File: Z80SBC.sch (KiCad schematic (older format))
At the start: 52 parts, among them IC1 SIO2-DIP-40, IC2 Z80CPU-DIP, J1 PH, J2 DB9_Female, J3 CFCONN, J4 Barrel_Jack, SW1 SW_Push, SW2 SW_Push, U1 MAX232_ALT, U2 74LS138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

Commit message: revised README.md
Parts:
- removed C13: 100 nF, Capacitors_THT:C_Disc_D5.0mm_W2.5mm_P5.00mm, symbol C_Small
- removed JP2: HCT/TTL, Pin_Headers:Pin_Header_Straight_1x03_Pitch2.54mm, symbol Jumper_NC_Dual
- removed R11: R, Resistors_THT:R_Axial_DIN0207_L6.3mm_D2.5mm_P7.62mm_Horizontal, symbol R
- removed R12: 1k, Resistors_THT:R_Axial_DIN0207_L6.3mm_D2.5mm_P7.62mm_Horizontal, symbol R
- removed U4: 27128, symbol 27128
- added C20, C21, C22, C23, C24, C25: 100 nF, Capacitors_THT:C_Disc_D5.0mm_W2.5mm_P2.50mm, symbol C_Small
- added JP6: Jumper_NC_Dual, Pin_Headers:Pin_Header_Straight_1x03_Pitch2.54mm, symbol Jumper_NC_Dual
- added U4: 28C256, Housings_DIP:DIP-28_W15.24mm_Socket, symbol 28C256
- C10, C11, C12, C8, C9: footprint Capacitors_THT:C_Disc_D5.0mm_W2.5mm_P5.00mm -> Capacitors_THT:C_Disc_D5.0mm_W2.5mm_P2.50mm
- C5, C6: value C -> 22 pF
- J3: footprint Pin_Headers:Pin_Header_Straight_2x25_Pitch1.27mm -> Z80:Pin_Header_Straight_2x25_Pitch1.27mm_Rev
- J4: footprint (none) -> Connectors:BARREL_JACK
- R6: value R -> 1M
- U1, U2: footprint (none) -> Housings_DIP:DIP-16_W7.62mm_Socket
- U6, U8: value 74LS32 -> 74HCT32
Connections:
- net labels added: IO08-0F, IO18-1F, IO20-27, IO28-2F, IO30-37, VCC
- net labels removed: ENABLEROM
- wire segments 285 -> 249
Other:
- note added: "Z80 CPM COMPUTER SYSTEM\nBASED ON 9 CHIP CP/M COMPUTER BY GRANT SEARLE\n"
- note removed: "R6/R11 1 M 74HCT00 / 330 ohm 74LS00\nC5 22 pF 74HCT 00/ 120 pF 74LS00\nC6 22 pF 74HCT00 / NC 74LS00\nJP2 1-2 74HCT00 / 2-3 74LS00"
- note removed: "Z80 CPM COMPUTER SYSTEM\n9 CHIP\nORIGINAL DESIGN BY GRANT SEARLE\n"
- moved on the sheet: C5, C6, R6, U2, U6A, U6B, U6C, U6D, U7A, U7B, U7C, U7D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

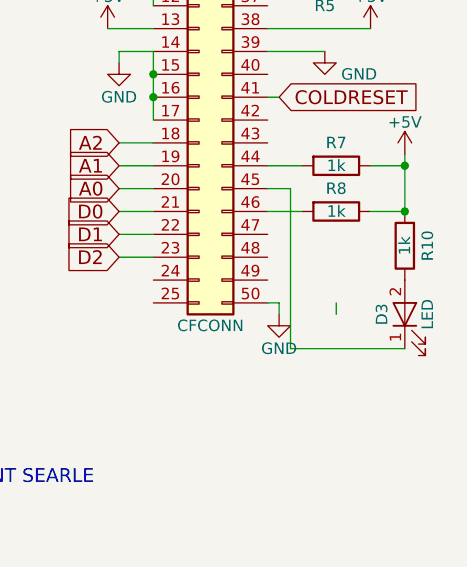
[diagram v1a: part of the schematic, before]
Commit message: Added PS/2 keyboard input
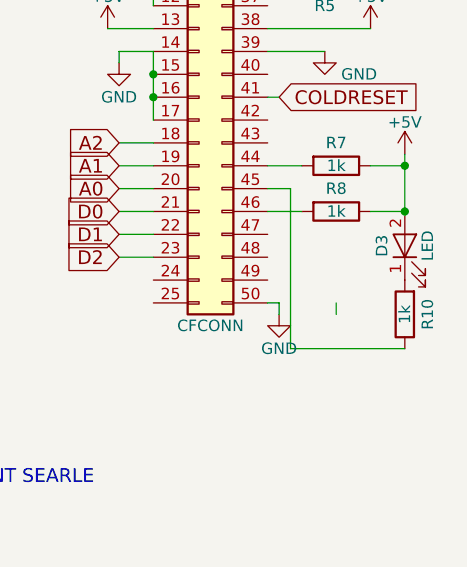
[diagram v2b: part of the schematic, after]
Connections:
- net +5V: now also D3.2 (A); no longer R10.2
- net at J3.45 (Pin_45): now also R10.1; no longer D3.1 (K)
- new net: D3.1 (K), R10.2
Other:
- moved on the sheet: D3, R10

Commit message: Added ESP-01 and video output
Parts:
- removed IC1: SIO2-DIP-40, Housings_DIP:DIP-40_W15.24mm_Socket, symbol SIO2-DIP-40
- added C32: 100 nF, Capacitors_THT:C_Disc_D5.0mm_W2.5mm_P2.50mm, symbol C_Small
- added D10, D9: 1N4148, Diodes_THT:D_DO-35_SOD27_P7.62mm_Horizontal, symbol D
- added IC1: DART-DIP-40, Housings_DIP:DIP-40_W15.24mm_Socket, symbol DART-DIP-40
- added J15: Conn_02x04_Odd_Even, Z80:Pin_Header_Straight_2x04_Pitch2.54mm_Flipped, symbol Conn_02x04_Odd_Even
- added JP7: Jumper_NC_Dual, Pin_Headers:Pin_Header_Straight_1x03_Pitch2.54mm, symbol Jumper_NC_Dual
- added R32: 470R, Resistors_THT:R_Axial_DIN0207_L6.3mm_D2.5mm_P7.62mm_Horizontal, symbol R
- added R33: 1k, Resistors_THT:R_Axial_DIN0207_L6.3mm_D2.5mm_P7.62mm_Horizontal, symbol R
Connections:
- net +5V: now also D9.2 (A), IC1.6 (IEI), IC1.9 (+5V), JP7.3
- net A0: now also IC1.34 (B/~A)
- net A1: now also IC1.33 (C/~D)
- net A14: now also JP7.1; no longer U4.1 (A14)
- net CLK: now also IC1.13 (~RXCA), IC1.14 (~TXCA), IC1.20 (Φ), IC1.27 (~RxTxCB)
- net COLDRESET: now also IC1.21 (~RESET)
- net D0: now also IC1.40 (D0)
- net D1: now also IC1.1 (D1)
- net D2: now also IC1.39 (D2)
- net D3: now also IC1.2 (D3)
- net D4: now also IC1.38 (D4)
- net D5: now also IC1.3 (D5)
- net D6: now also IC1.37 (D6)
- net D7: now also IC1.4 (D7)
- net GND: now also C32.2, IC1.19 (~DCDA), IC1.22 (~DCDB), IC1.23 (~CTSB), IC1.31 (GND), J15.1 (Pin_1), R33.1
- net INT: now also IC1.5 (~INT)
- net IO00-07: now also IC1.35 (~CE)
- net IORQ: now also IC1.36 (~IORQ)
- net M1: now also IC1.8 (~M1)
- net RD: now also IC1.32 (~RD)
- net RTSB: now also IC1.24 (~RTSB)
- net RXDB: now also IC1.28 (RXDB)
- net TXDB: now also IC1.26 (TXDB)
- net at J1.6 (Pin_6): now also IC1.12 (RXDA), J15.2 (Pin_2)
- net at J1.5 (Pin_5): now also IC1.15 (TXDA), R32.2
- net at J1.2 (Pin_2): now also IC1.16 (~DTRA)
- net at J1.4 (Pin_4): now also IC1.17 (~RTSA)
- net at J1.3 (Pin_3), JP1.2: now also IC1.18 (~CTSA)
- new net: J15.7 (Pin_7), R32.1, R33.2
- new net: C32.1, D10.1 (K), J15.8 (Pin_8)
- new net: D10.2 (A), D9.1 (K)
- new net R14: JP7.2, U4.1 (A14)
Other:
- moved on the sheet: C5, C6, JP1, R6, U7A, U7B, Y1

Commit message: Fixed jumpers, CF card position, ESP-01 enable
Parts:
- added R?: 10k, Resistors_THT:R_Axial_DIN0207_L6.3mm_D2.5mm_P7.62mm_Horizontal, symbol R
- R32: value 470R -> 4k7
- R33: value 1k -> 10k
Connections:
- net +5V: no longer JP6.3
- net GND: now also JP6.3
- net at J15.4 (Pin_4): now also R?.1
- net at C32.1, D10.1 (K), J15.8 (Pin_8): now also R?.2
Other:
- note added: "Z8470BPS"

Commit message: Added SD card driver
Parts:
- gave numbers to parts that had none: 1
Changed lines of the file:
@@
 $EndComp
 $Comp
-L R R?
+L R R37
 U 1 1 61062DF7
 P 1650 2400
-F 0 "R?" V 1550 2350 50  0000 C CNN
+F 0 "R37" V 1550 2350 50  0000 C CNN
 F 1 "10k" V 1650 2400 50  0000 C CNN
 F 2 "Resistors_THT:R_Axial_DIN0207_L6.3mm_D2.5mm_P7.62mm_Horizontal" V 1580 2400 50  0001 C CNN

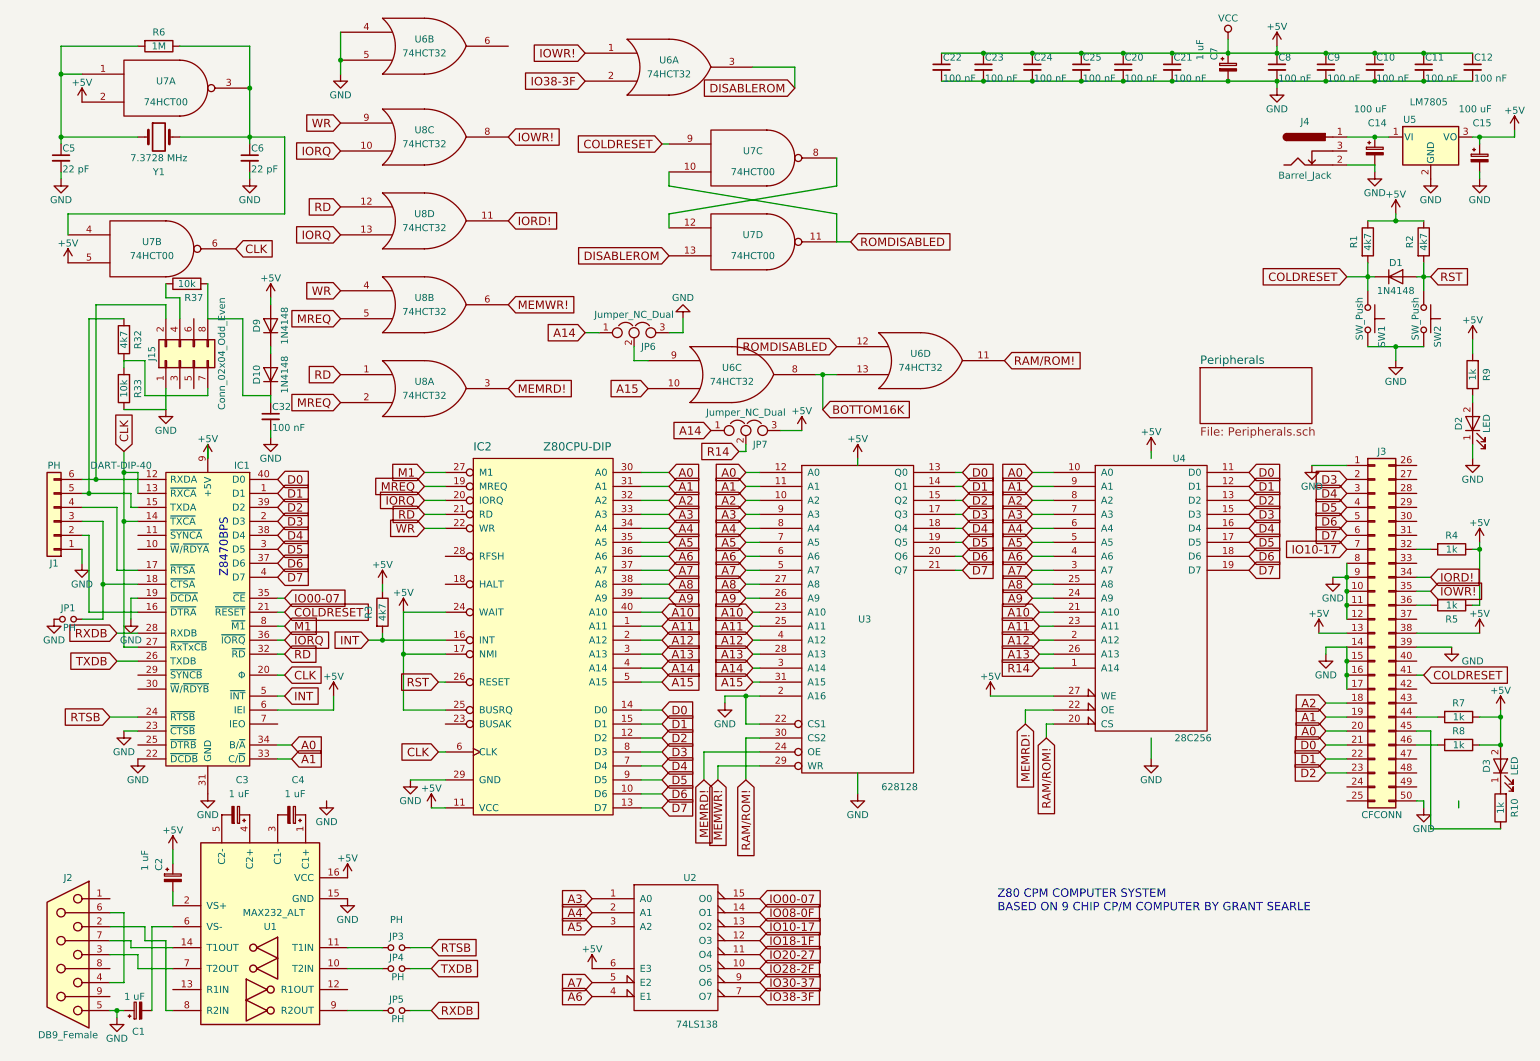
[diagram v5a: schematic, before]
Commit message: Fixed PS/2 interrupt line
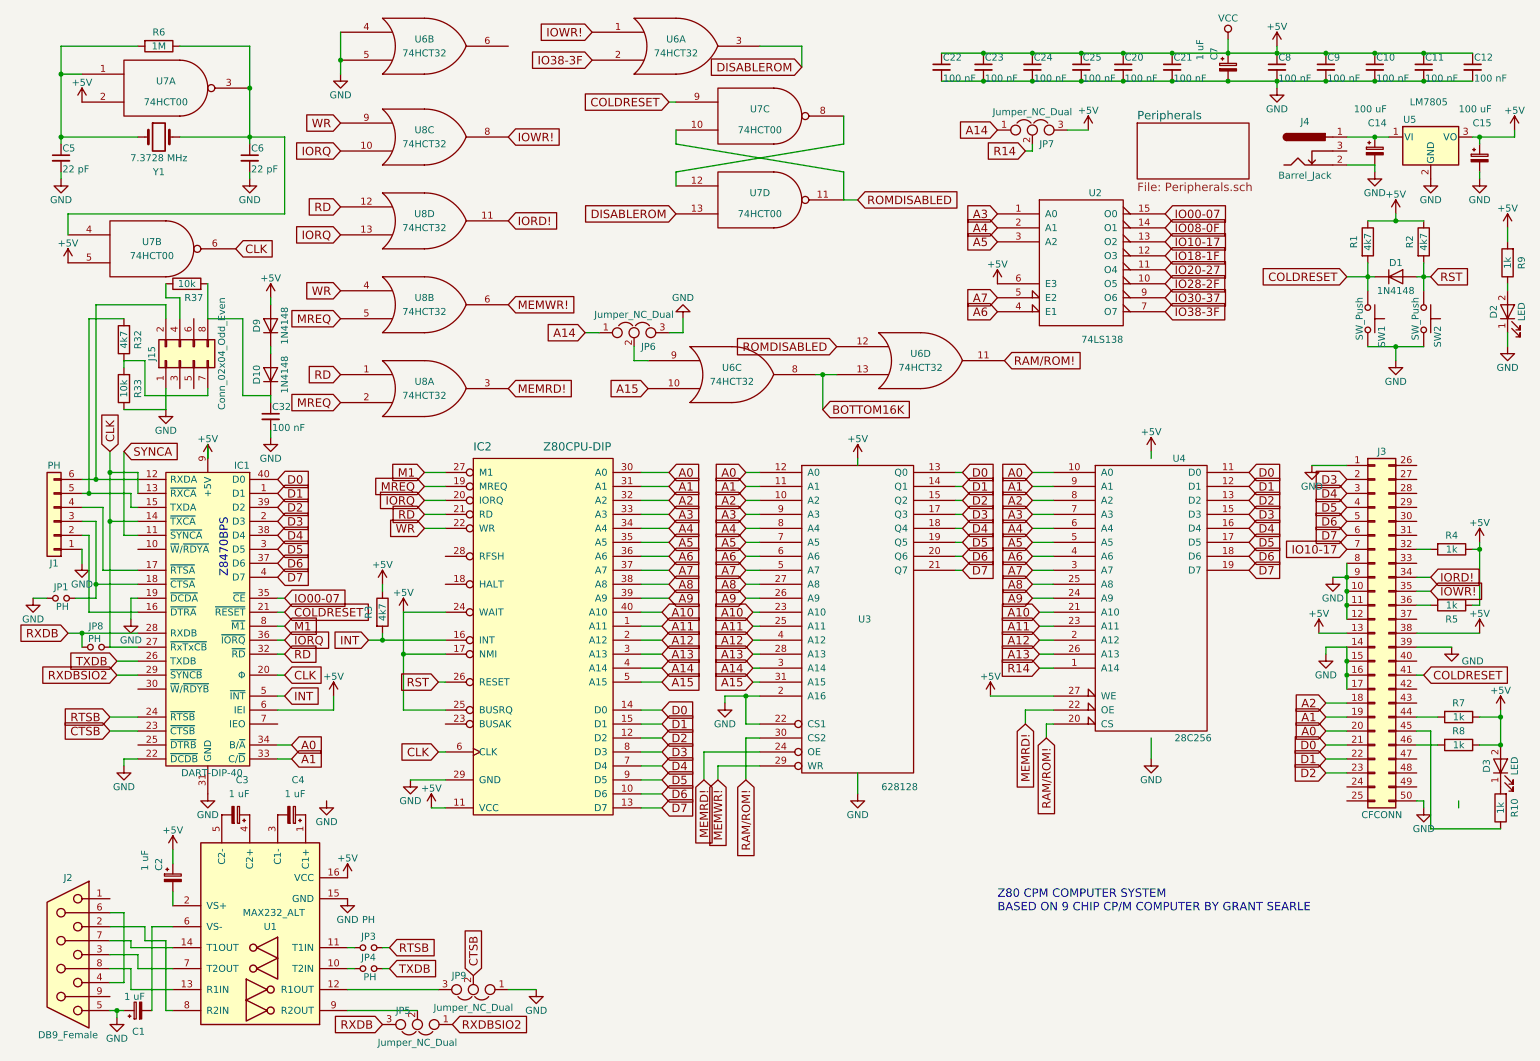
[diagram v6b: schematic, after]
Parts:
- removed JP5: PH, Pin_Headers:Pin_Header_Straight_1x02_Pitch2.54mm, symbol Jumper_NO_Small
- added JP5, JP9: Jumper_NC_Dual, Pin_Headers:Pin_Header_Straight_1x03_Pitch2.54mm, symbol Jumper_NC_Dual
- added JP8: PH, Pin_Headers:Pin_Header_Straight_1x02_Pitch2.54mm, symbol Jumper_NO_Small
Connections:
- net CLK: now also JP8.1
- net GND: now also JP9.1; no longer IC1.23 (~CTSB)
- net RXDB: now also JP5.3, JP8.2
- net at J2.8: now also U1.13 (R1IN)
- net at U1.12 (R1OUT): now also JP9.3
- net at U1.9 (R2OUT): now also JP5.2
- net SYNCA: now reaches IC1.11 (~SYNCA)
- net RXDBSIO2: now reaches IC1.29 (~SYNCB)
- net RXDBSIO2: now also JP5.1
- new net CTSB: IC1.23 (~CTSB), JP9.2
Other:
- moved on the sheet: D2, JP1, JP3, JP4, JP7, R9, U2, U6A, U7C, U7D

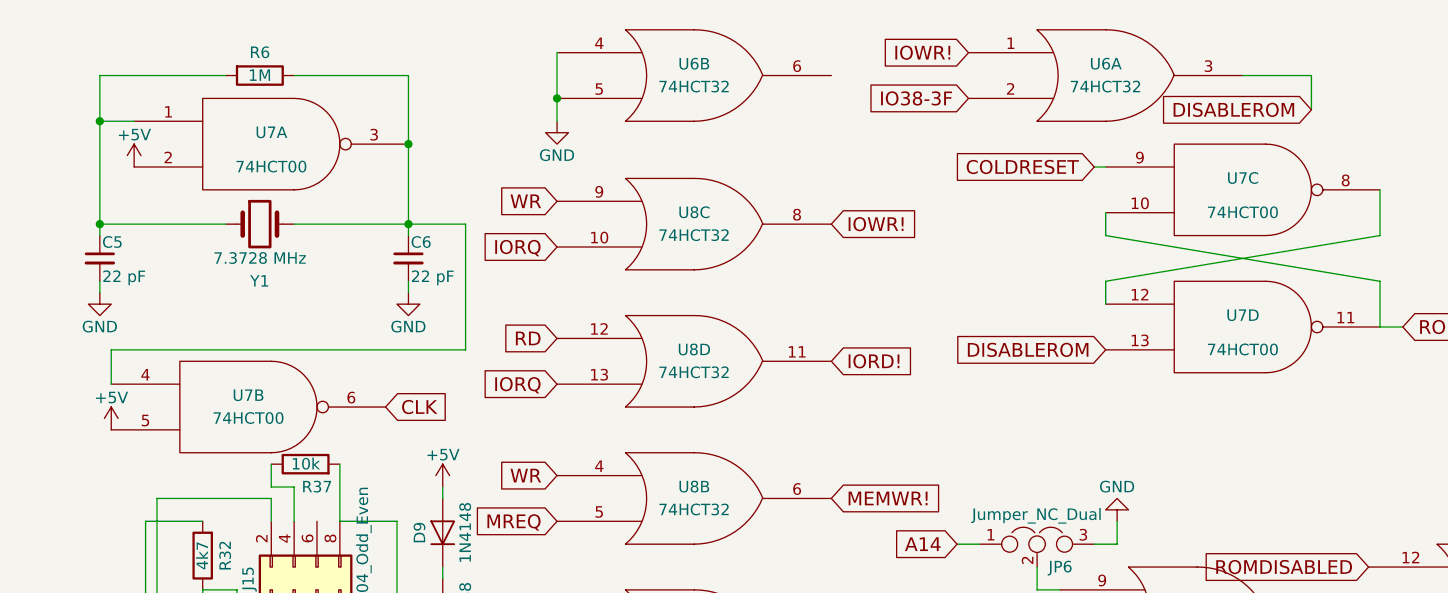
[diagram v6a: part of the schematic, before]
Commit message: Fixed SDHC support, added extra configuration jumpers
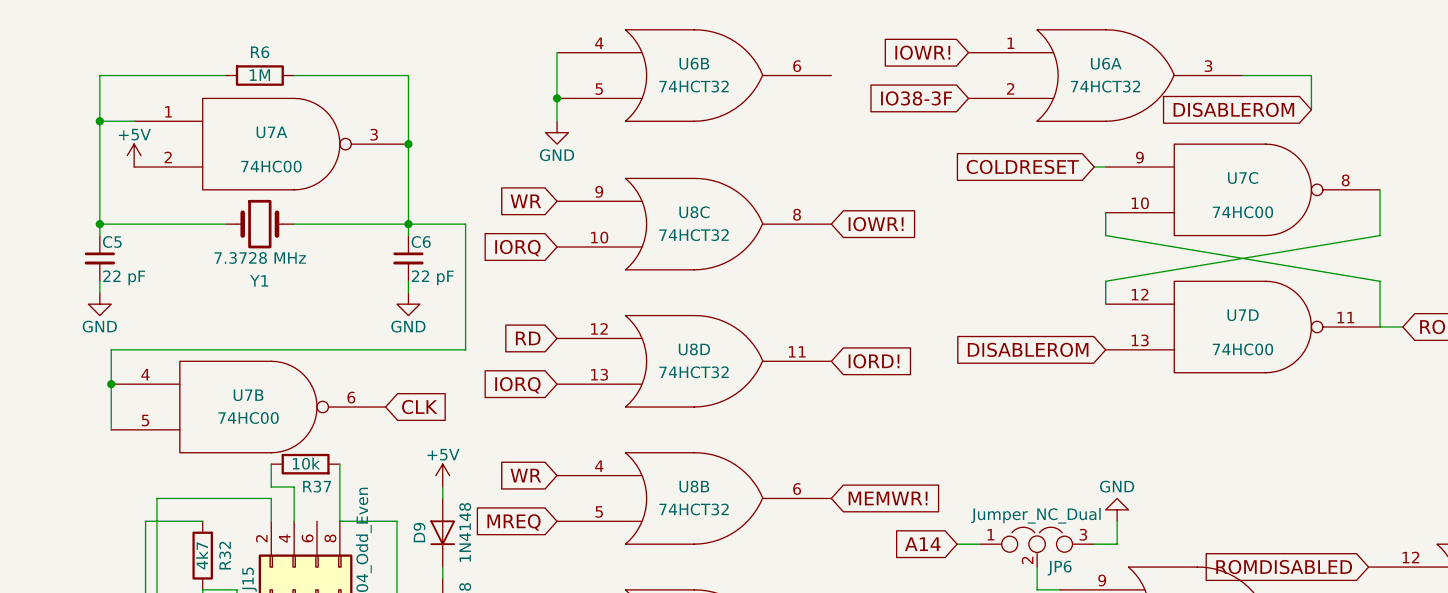
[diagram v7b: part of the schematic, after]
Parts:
- U7: value 74HCT00 -> 74HC00
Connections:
- net +5V: no longer U7.5
- net at C6.1, R6.1, U7.3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: now also U7.5
